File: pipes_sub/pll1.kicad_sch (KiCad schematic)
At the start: 86 parts, among them U1 CD4046, U10 CD4046, U11 CD4046, U13 CD4017, U15 CD4017, U3 CD4017, U5 CD4046, U6 TL072CP, U8 CD4017, U9 TL072CP

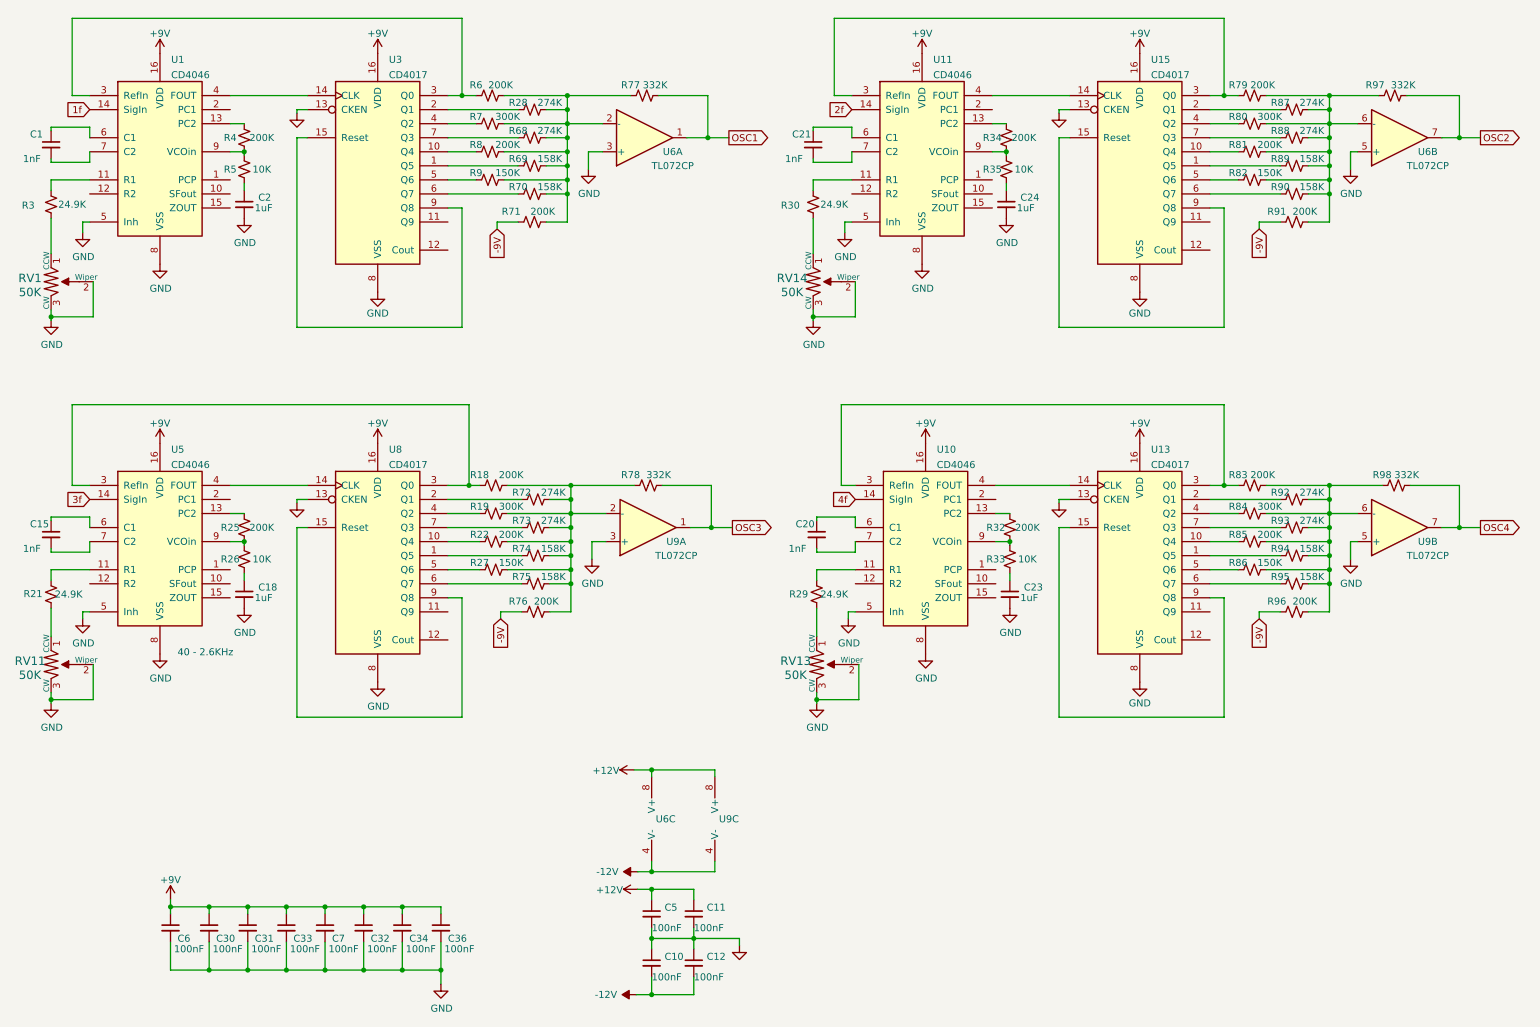
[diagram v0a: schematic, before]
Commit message: Adds digikey bom merge. Uses local graphics for panel.
Adds bambooh graphics
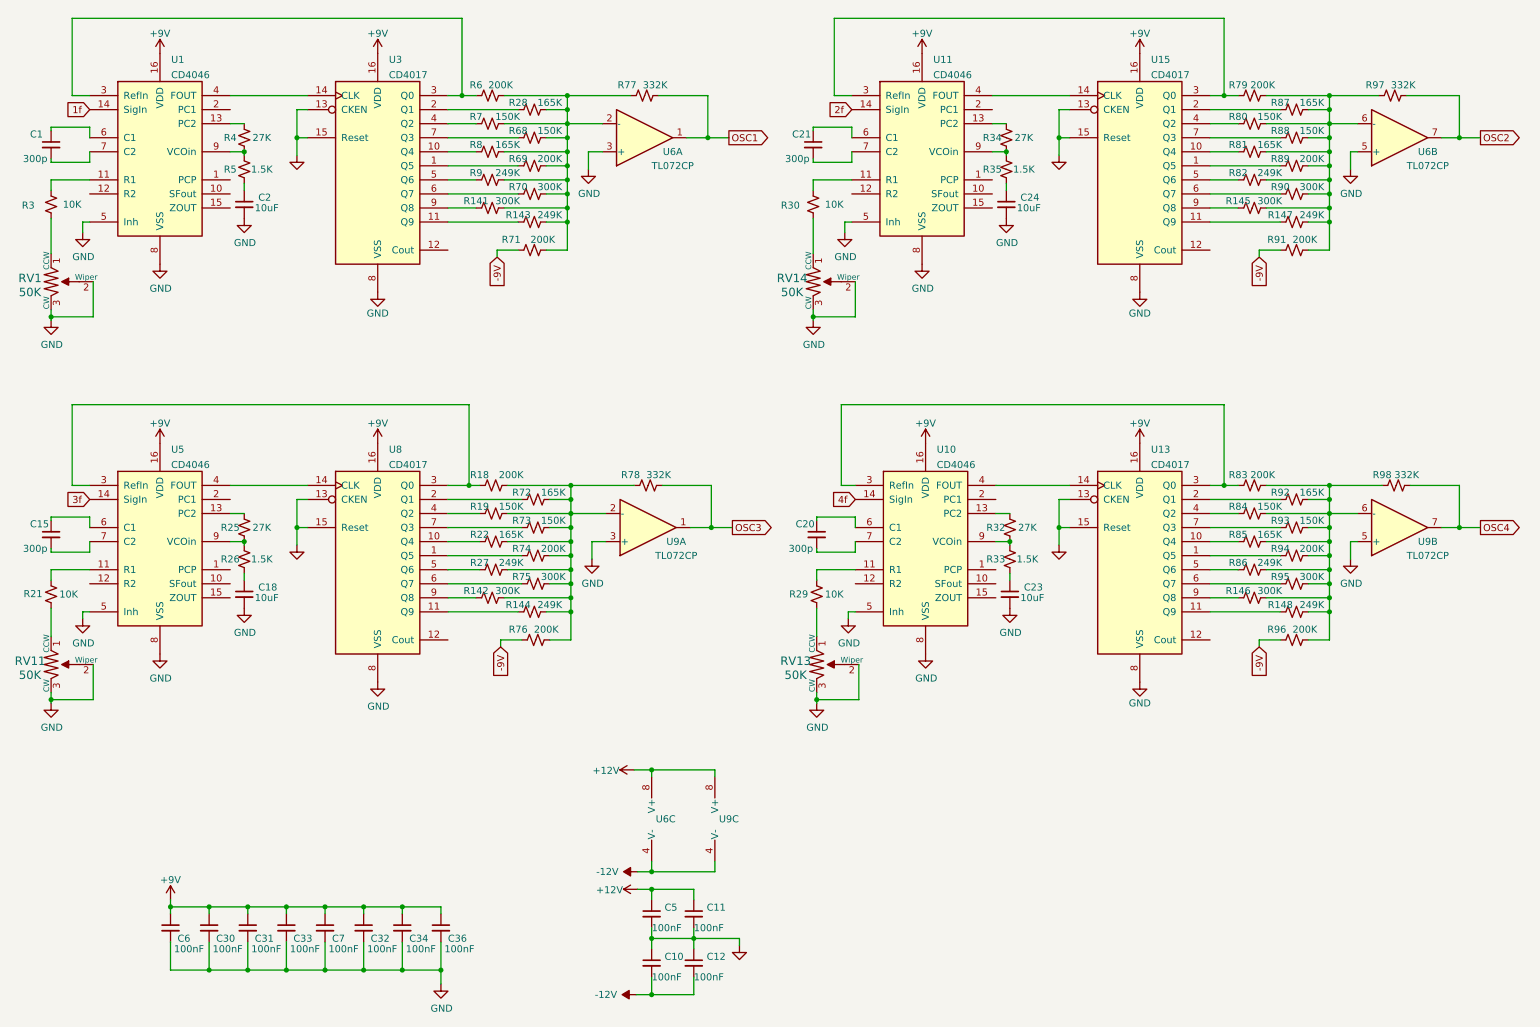
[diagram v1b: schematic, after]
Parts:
- added R141, R142, R145, R146: 300K, Resistor_SMD:R_0603_1608Metric, symbol Device:R_Small_US
- added R143, R144, R147, R148: 249K, Resistor_SMD:R_0603_1608Metric, symbol Device:R_Small_US
- C1, C15, C20, C21: value 1nF -> 300p; LCSC Part # C46653 -> C282698
- C18, C2, C23, C24: value 1uF -> 10uF; LCSC Part # C28323 -> C15850
- R19, R7, R80, R84: value 300K -> 150K; LCSC Part # C23024 -> C22807
- R21, R29, R3, R30: value 24.9K -> 10K; LCSC Part # C137761 -> C25804
- R22, R8, R81, R85: value 200K -> 165K; LCSC Part # C25811 -> C308203
- R25, R32, R34, R4: value 200K -> 27K; LCSC Part # C17539 -> C17593
- R26, R33, R35, R5: value 10K -> 1.5K; LCSC Part # C17414 -> C4310
- R27, R82, R86, R9: value 150K -> 249K; LCSC Part # C22807 -> C311921
- R28, R72, R87, R92: value 274K -> 165K; LCSC Part # C227748 -> C308203
- R68, R73, R88, R93: value 274K -> 150K; LCSC Part # C227748 -> C22807
- R69, R74, R89, R94: value 158K -> 200K; LCSC Part # C273745 -> C25811
- R70, R75, R90, R95: value 158K -> 300K; LCSC Part # C273745 -> C23024
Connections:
- net GND: now also U13.15 (Reset), U15.15 (Reset), U3.15 (Reset), U8.15 (Reset)
- net at R79.2, R80.2, R81.2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: now also R145.2, R147.2
- net at R83.2, R84.2, R85.2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: now also R146.2, R148.2
- net at R28.2, R6.2, R68.2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: now also R141.2, R143.2
- net at R18.2, R19.2, R22.2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: now also R142.2, R144.2
- net at U15.11 (Q9): now also R147.1
- net at U15.9 (Q8): now also R145.1; no longer U15.15 (Reset)
- net at U8.11 (Q9): now also R144.1
- net at U8.9 (Q8): now also R142.1; no longer U8.15 (Reset)
- net at U3.11 (Q9): now also R143.1
- net at U3.9 (Q8): now also R141.1; no longer U3.15 (Reset)
- net at U13.11 (Q9): now also R148.1
- net at U13.9 (Q8): now also R146.1; no longer U13.15 (Reset)
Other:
- note removed: "40 - 2.6KHz"
- moved on the sheet: R71, R76, R91, R96

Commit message: Version 1.1 of boards
Changes to use NSL-32SR3 Vactrols
Fixes 3904 package
Adds 10-step waveform
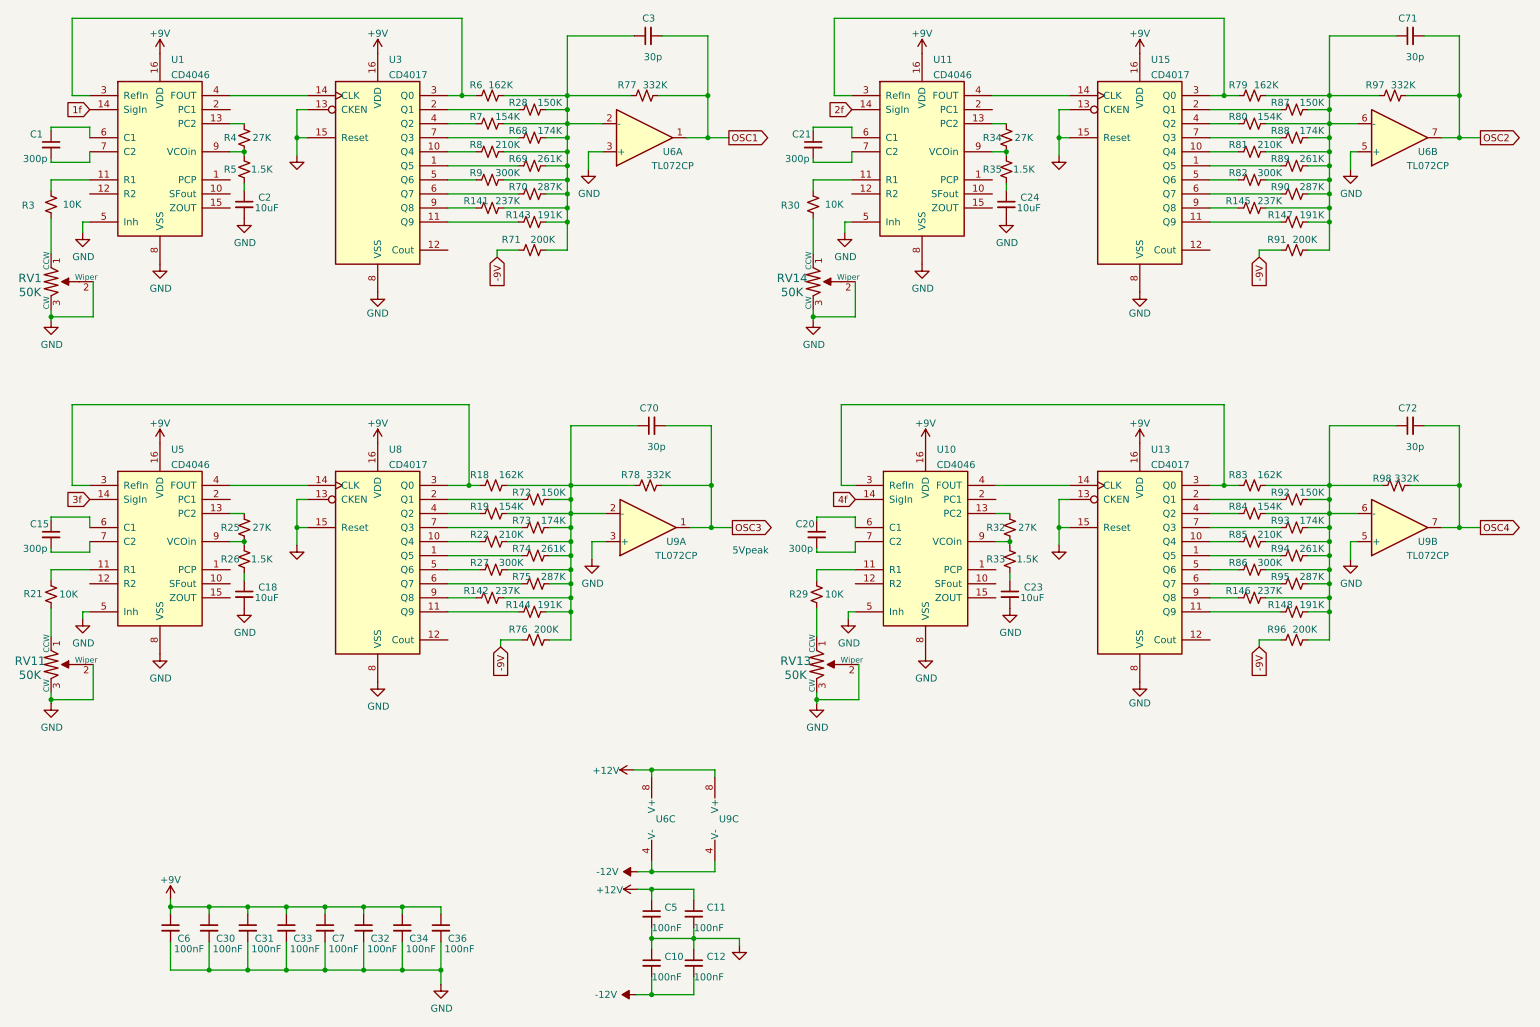
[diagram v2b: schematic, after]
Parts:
- added C3, C70, C71, C72: 30p, Capacitor_SMD:C_0805_2012Metric_Pad1.18x1.45mm_HandSolder, symbol Device:C_Small
- R141, R142, R145, R146: value 300K -> 237K; LCSC Part # C23024 -> C403089
- R143, R144, R147, R148: value 249K -> 191K; LCSC Part # C311921 -> C861179
- R18, R6, R79, R83: value 200K -> 162K; LCSC Part # C25811 -> C217756
- R19, R7, R80, R84: value 150K -> 154K; LCSC Part # C22807 -> C321731
- R22, R8, R81, R85: value 165K -> 210K; LCSC Part # C308203 -> C227705
- R27, R82, R86, R9: value 249K -> 300K; LCSC Part # C311921 -> C23024
- R28, R72, R87, R92: value 165K -> 150K; LCSC Part # C308203 -> C22807
- R68, R73, R88, R93: value 150K -> 174K; LCSC Part # C22807 -> C2933159
- R69, R74, R89, R94: value 200K -> 261K; LCSC Part # C25811 -> C2930083
- R70, R75, R90, R95: value 300K -> 287K; LCSC Part # C23024 -> C5159700
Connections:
- net OSC1: now also C3.2
- net OSC2: now also C71.2
- net OSC3: now also C70.2
- net OSC4: now also C72.2
- net at R145.2, R147.2, R79.2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: now also C71.1
- net at R146.2, R148.2, R83.2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: now also C72.1
- net at R142.2, R144.2, R18.2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: now also C70.1
- net at R141.2, R143.2, R28.2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: now also C3.1
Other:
- note added: "5Vpeak"
